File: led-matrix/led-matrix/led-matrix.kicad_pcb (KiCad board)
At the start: 4 copper layers, 300 parts, among them J1 Conn_2Rows-05Pins, Q1 2N7002, Q10 2N7002, Q11 2N7002, Q12 2N7002, Q13 2N7002, Q14 2N7002, Q15 2N7002, Q16 2N7002, Q2 2N7002, Q3 2N7002, Q4 2N7002, Q5 2N7002, Q6 2N7002, Q7 2N7002, Q8 2N7002, Q9 2N7002, U1 74LS595, U2 74LS595, U3 74LS595, U4 74LS595, U5 AMS1117-3.3

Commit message: Improved annotations and board layout
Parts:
- removed the D257 at (266.6, 236.1)
- added C5: C, Capacitor_SMD:C_0603_1608Metric, B.Cu at (26.7, 66.0)
- added C6: C, Capacitor_SMD:C_0603_1608Metric, B.Cu at (22.9, 73.7)
- added D2: LED, LED_SMD:LED_0603_1608Metric, F.Cu at (193.0, 29.2)
- added J1: Conn_2Rows-05Pins, Connector_PinHeader_1.00mm:PinHeader_1x05_P1.00mm_Horizontal, F.Cu at (7.62, 66.0)
- C1, C2, C3, C4, F1, Q11, Q6, R1, R10, R11, R12, R13, R14, R15, R16, R2, R3, R4, R5, R6, R7, R8, R9, U1, U5: moved to B.Cu
- D257: renamed from D2; moved to B.Cu
- Q1: renamed from Q16; moved to B.Cu
- Q10: renamed from Q13; moved to B.Cu
- Q12: renamed from Q9; moved to B.Cu
- Q13: renamed from Q7; moved to B.Cu
- Q14: renamed from Q5; moved to B.Cu
- Q15: renamed from Q3; moved to B.Cu
- Q16: renamed from Q1; moved to B.Cu
- Q2: renamed from Q14; moved to B.Cu
- Q3: renamed from Q12; moved to B.Cu
- Q4: renamed from Q10; moved to B.Cu
- Q5: renamed from Q8; moved to B.Cu
- Q7: renamed from Q4; moved to B.Cu
- Q8: renamed from Q2; moved to B.Cu
- Q9: renamed from Q15; moved to B.Cu
- U2: renamed from U4; moved to B.Cu
- U3: renamed from U2; moved to B.Cu
- U4: renamed from U3; moved to B.Cu
- moved D64 237.4 mm to (250.5, 44.5), turned to 90 degrees
- moved D29 236.5 mm to (232.8, 33.5), turned to 90 degrees
- moved D59 234.8 mm to (228.4, 44.5), turned to 90 degrees
- moved D47 234.6 mm to (241.3, 39.4), turned to 90 degrees
- moved D14 234.5 mm to (237.7, 29.2), turned to 90 degrees
- moved D43 234.2 mm to (226.1, 39.4), turned to 90 degrees
- moved D16 233.0 mm to (245.1, 29.2), turned to 90 degrees
- moved D24 230.0 mm to (215.2, 33.5), turned to 90 degrees
- moved D10 228.2 mm to (222.8, 29.2), turned to 90 degrees
- moved D26 228.0 mm to (222.2, 33.5), turned to 90 degrees
- moved D30 227.8 mm to (236.3, 33.5), turned to 90 degrees
- moved D36 226.7 mm to (198.1, 39.4), turned to 90 degrees
- moved D12 226.5 mm to (230.2, 29.2), turned to 90 degrees
- moved D60 226.4 mm to (232.8, 44.5), turned to 90 degrees
- moved D63 226.3 mm to (246.1, 44.5), turned to 90 degrees
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- renumbered J1 to J2
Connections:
- D105 pad 1: Net-(D10-Pad1) -> Net-(D105-Pad1)
- D106 pad 1: Net-(D106-Pad1) -> Net-(D10-Pad1)
- D11 pad 1: Net-(D104-Pad1) -> Net-(D107-Pad1)
- D113 pad 2: ROW6 -> ROW7
- D12 pad 1: Net-(D103-Pad1) -> Net-(D108-Pad1)
- D121 pad 1: Net-(D10-Pad1) -> Net-(D105-Pad1)
- D122 pad 1: Net-(D106-Pad1) -> Net-(D10-Pad1)
- D129 pad 2: ROW7 -> ROW8
- D13 pad 1: Net-(D102-Pad1) -> Net-(D109-Pad1)
- D137 pad 1: Net-(D10-Pad1) -> Net-(D105-Pad1)
- D138 pad 1: Net-(D106-Pad1) -> Net-(D10-Pad1)
- D14 pad 1: Net-(D101-Pad1) -> Net-(D110-Pad1)
- D145 pad 2: ROW8 -> ROW9
- D15 pad 1: Net-(D100-Pad1) -> Net-(D111-Pad1)
- D153 pad 1: Net-(D10-Pad1) -> Net-(D105-Pad1)
- D154 pad 1: Net-(D106-Pad1) -> Net-(D10-Pad1)
- D16 pad 1: Net-(D115-Pad1) -> Net-(D112-Pad1)
- D161 pad 2: ROW9 -> ROW10
- D169 pad 1: Net-(D10-Pad1) -> Net-(D105-Pad1)
- D17 pad 1: Net-(D114-Pad1) -> Net-(D1-Pad1)
- D17 pad 2: ROW0 -> ROW1
- D170 pad 1: Net-(D106-Pad1) -> Net-(D10-Pad1)
- D177 pad 2: ROW10 -> ROW11
- D18 pad 1: Net-(D1-Pad1) -> Net-(D114-Pad1)
- D185 pad 1: Net-(D10-Pad1) -> Net-(D105-Pad1)
- D186 pad 1: Net-(D106-Pad1) -> Net-(D10-Pad1)
- D19 pad 1: Net-(D112-Pad1) -> Net-(D115-Pad1)
- D193 pad 2: ROW11 -> ROW12
- D20 pad 1: Net-(D111-Pad1) -> Net-(D100-Pad1)
- D201 pad 1: Net-(D10-Pad1) -> Net-(D105-Pad1)
- D202 pad 1: Net-(D106-Pad1) -> Net-(D10-Pad1)
- D209 pad 2: ROW12 -> ROW13
- D21 pad 1: Net-(D110-Pad1) -> Net-(D101-Pad1)
- D217 pad 1: Net-(D10-Pad1) -> Net-(D105-Pad1)
- D218 pad 1: Net-(D106-Pad1) -> Net-(D10-Pad1)
- D22 pad 1: Net-(D109-Pad1) -> Net-(D102-Pad1)
- D225 pad 2: ROW13 -> ROW14
- D23 pad 1: Net-(D108-Pad1) -> Net-(D103-Pad1)
- D233 pad 1: Net-(D10-Pad1) -> Net-(D105-Pad1)
- D234 pad 1: Net-(D106-Pad1) -> Net-(D10-Pad1)
- D24 pad 1: Net-(D107-Pad1) -> Net-(D104-Pad1)
- D241 pad 2: ROW14 -> ROW15
- D249 pad 1: Net-(D10-Pad1) -> Net-(D105-Pad1)
- D25 pad 1: Net-(D106-Pad1) -> Net-(D105-Pad1)
- D250 pad 1: Net-(D106-Pad1) -> Net-(D10-Pad1)
- D27 pad 1: Net-(D104-Pad1) -> Net-(D107-Pad1)
- D28 pad 1: Net-(D103-Pad1) -> Net-(D108-Pad1)
- D29 pad 1: Net-(D102-Pad1) -> Net-(D109-Pad1)
- D3 pad 1: Net-(D112-Pad1) -> Net-(D115-Pad1)
- D30 pad 1: Net-(D101-Pad1) -> Net-(D110-Pad1)
- D31 pad 1: Net-(D100-Pad1) -> Net-(D111-Pad1)
- D32 pad 1: Net-(D115-Pad1) -> Net-(D112-Pad1)
- D33 pad 1: Net-(D114-Pad1) -> Net-(D1-Pad1)
- D33 pad 2: ROW1 -> ROW2
- D34 pad 1: Net-(D1-Pad1) -> Net-(D114-Pad1)
- D35 pad 1: Net-(D112-Pad1) -> Net-(D115-Pad1)
- D36 pad 1: Net-(D111-Pad1) -> Net-(D100-Pad1)
- D37 pad 1: Net-(D110-Pad1) -> Net-(D101-Pad1)
- D38 pad 1: Net-(D109-Pad1) -> Net-(D102-Pad1)
- D39 pad 1: Net-(D108-Pad1) -> Net-(D103-Pad1)
- D4 pad 1: Net-(D111-Pad1) -> Net-(D100-Pad1)
- D40 pad 1: Net-(D107-Pad1) -> Net-(D104-Pad1)
- D41 pad 1: Net-(D106-Pad1) -> Net-(D105-Pad1)
- D43 pad 1: Net-(D104-Pad1) -> Net-(D107-Pad1)
- D44 pad 1: Net-(D103-Pad1) -> Net-(D108-Pad1)
- D45 pad 1: Net-(D102-Pad1) -> Net-(D109-Pad1)
- D46 pad 1: Net-(D101-Pad1) -> Net-(D110-Pad1)
- D47 pad 1: Net-(D100-Pad1) -> Net-(D111-Pad1)
- D48 pad 1: Net-(D115-Pad1) -> Net-(D112-Pad1)
- D49 pad 1: Net-(D114-Pad1) -> Net-(D1-Pad1)
- D49 pad 2: ROW2 -> ROW3
- D5 pad 1: Net-(D110-Pad1) -> Net-(D101-Pad1)
- D50 pad 1: Net-(D1-Pad1) -> Net-(D114-Pad1)
- D51 pad 1: Net-(D112-Pad1) -> Net-(D115-Pad1)
- D52 pad 1: Net-(D111-Pad1) -> Net-(D100-Pad1)
- D53 pad 1: Net-(D110-Pad1) -> Net-(D101-Pad1)
- D54 pad 1: Net-(D109-Pad1) -> Net-(D102-Pad1)
- D55 pad 1: Net-(D108-Pad1) -> Net-(D103-Pad1)
- D56 pad 1: Net-(D107-Pad1) -> Net-(D104-Pad1)
- D57 pad 1: Net-(D106-Pad1) -> Net-(D105-Pad1)
- D59 pad 1: Net-(D104-Pad1) -> Net-(D107-Pad1)
- D6 pad 1: Net-(D109-Pad1) -> Net-(D102-Pad1)
- D60 pad 1: Net-(D103-Pad1) -> Net-(D108-Pad1)
- D61 pad 1: Net-(D102-Pad1) -> Net-(D109-Pad1)
- D62 pad 1: Net-(D101-Pad1) -> Net-(D110-Pad1)
- D63 pad 1: Net-(D100-Pad1) -> Net-(D111-Pad1)
- D64 pad 1: Net-(D115-Pad1) -> Net-(D112-Pad1)
- D65 pad 1: Net-(D114-Pad1) -> Net-(D1-Pad1)
- D65 pad 2: ROW3 -> ROW4
- D66 pad 1: Net-(D1-Pad1) -> Net-(D114-Pad1)
- D67 pad 1: Net-(D112-Pad1) -> Net-(D115-Pad1)
- D68 pad 1: Net-(D111-Pad1) -> Net-(D100-Pad1)
- D69 pad 1: Net-(D110-Pad1) -> Net-(D101-Pad1)
- D7 pad 1: Net-(D108-Pad1) -> Net-(D103-Pad1)
- D70 pad 1: Net-(D109-Pad1) -> Net-(D102-Pad1)
- D71 pad 1: Net-(D108-Pad1) -> Net-(D103-Pad1)
- D72 pad 1: Net-(D107-Pad1) -> Net-(D104-Pad1)
- D73 pad 1: Net-(D106-Pad1) -> Net-(D105-Pad1)
- D75 pad 1: Net-(D104-Pad1) -> Net-(D107-Pad1)
- D76 pad 1: Net-(D103-Pad1) -> Net-(D108-Pad1)
- D77 pad 1: Net-(D102-Pad1) -> Net-(D109-Pad1)
- D78 pad 1: Net-(D101-Pad1) -> Net-(D110-Pad1)
- D79 pad 1: Net-(D100-Pad1) -> Net-(D111-Pad1)
- D8 pad 1: Net-(D107-Pad1) -> Net-(D104-Pad1)
- D80 pad 1: Net-(D115-Pad1) -> Net-(D112-Pad1)
- D81 pad 1: Net-(D114-Pad1) -> Net-(D1-Pad1)
- D81 pad 2: ROW4 -> ROW5
- D89 pad 1: Net-(D10-Pad1) -> Net-(D105-Pad1)
- D9 pad 1: Net-(D106-Pad1) -> Net-(D105-Pad1)
- D90 pad 1: Net-(D106-Pad1) -> Net-(D10-Pad1)
- D97 pad 2: ROW5 -> ROW6
- J2 pad 1: COLNEXT -> SERCOL
- J2 pad 3: ROWSEQ -> SERROW
- R10 pad 1: Net-(D104-Pad1) -> Net-(D10-Pad1)
- R11 pad 1: Net-(D103-Pad1) -> Net-(D107-Pad1)
- R12 pad 1: Net-(D102-Pad1) -> Net-(D108-Pad1)
- R13 pad 1: Net-(D101-Pad1) -> Net-(D109-Pad1)
- R14 pad 1: Net-(D100-Pad1) -> Net-(D110-Pad1)
- R15 pad 1: Net-(D115-Pad1) -> Net-(D111-Pad1)
- R16 pad 1: Net-(D114-Pad1) -> Net-(D112-Pad1)
- R2 pad 1: Net-(D112-Pad1) -> Net-(D114-Pad1)
- R3 pad 1: Net-(D111-Pad1) -> Net-(D115-Pad1)
- R4 pad 1: Net-(D110-Pad1) -> Net-(D100-Pad1)
- R5 pad 1: Net-(D109-Pad1) -> Net-(D101-Pad1)
- R6 pad 1: Net-(D108-Pad1) -> Net-(D102-Pad1)
- R7 pad 1: Net-(D107-Pad1) -> Net-(D103-Pad1)
- R8 pad 1: Net-(D106-Pad1) -> Net-(D104-Pad1)
- R9 pad 1: Net-(D10-Pad1) -> Net-(D105-Pad1)
- U1 pad 9: Net-(U1-Pad9) -> ROWNEXT
- U3 pad 9: Net-(U2-Pad9) -> COLNEXT
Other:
- board outline added: 88.9 x 77.5 mm

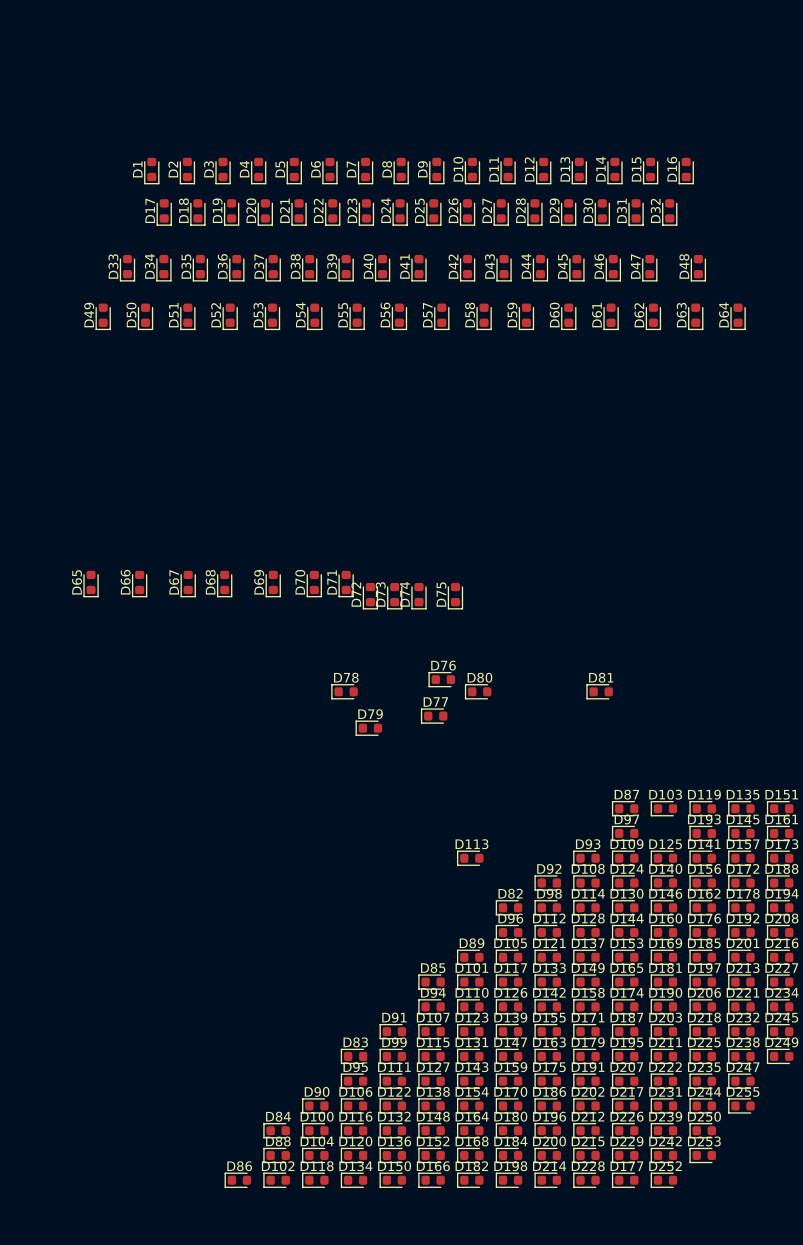
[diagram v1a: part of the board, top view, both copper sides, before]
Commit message: Updated layout
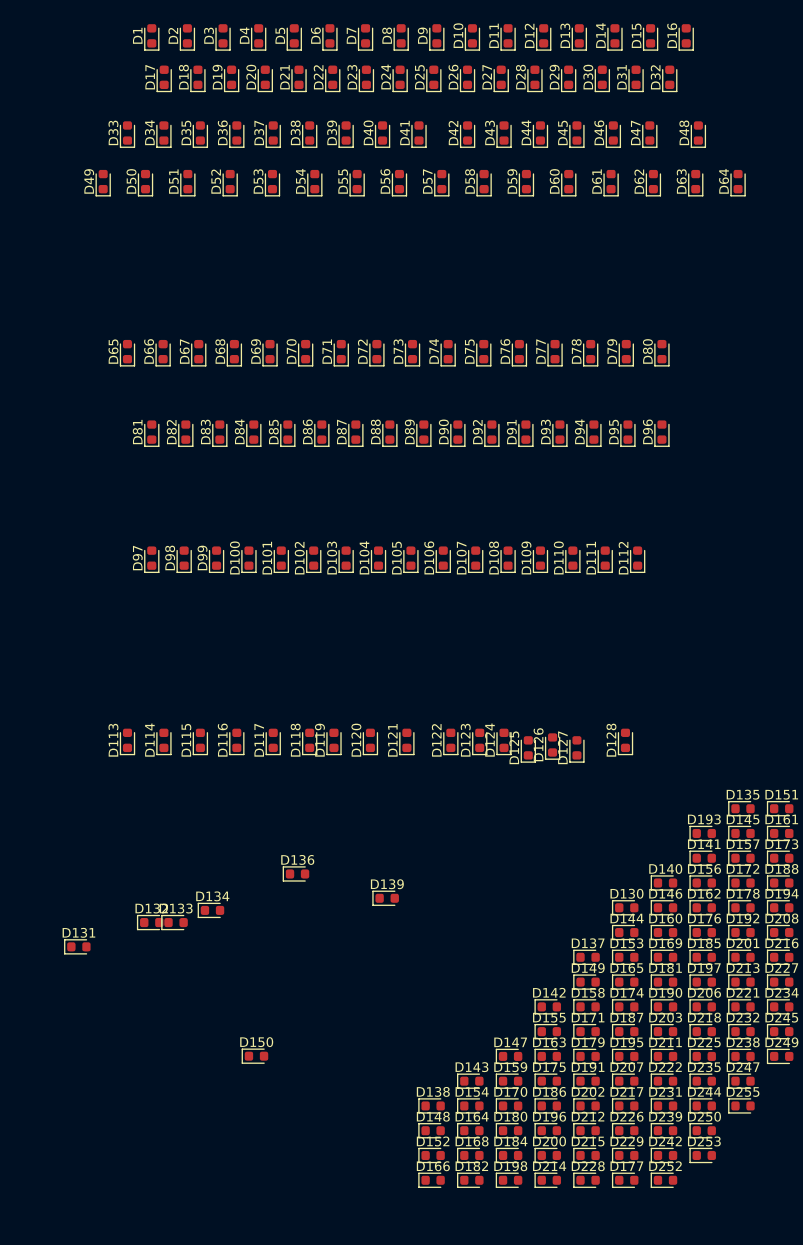
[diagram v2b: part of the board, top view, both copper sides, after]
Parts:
- moved D86 78.7 mm to (207.0, 56.7), turned to 90 degrees
- moved D88 76.5 mm to (214.1, 56.7), turned to 90 degrees
- moved D95 73.6 mm to (239.0, 56.7), turned to 90 degrees
- moved D84 73.1 mm to (199.9, 56.7), turned to 90 degrees
- moved D90 72.0 mm to (221.2, 56.7), turned to 90 degrees
- moved D83 66.8 mm to (196.3, 56.7), turned to 90 degrees
- moved D102 65.2 mm to (206.2, 69.8), turned to 90 degrees
- moved D91 64.2 mm to (228.3, 56.7), turned to 90 degrees
- moved D104 62.8 mm to (212.9, 69.8), turned to 90 degrees
- moved D94 62.4 mm to (235.5, 56.7), turned to 90 degrees
- moved D100 60.3 mm to (199.4, 69.8), turned to 90 degrees
- moved D82 60.2 mm to (192.8, 56.7), turned to 90 degrees
- moved D85 59.5 mm to (203.5, 56.7), turned to 90 degrees
- moved D111 59.0 mm to (236.6, 69.8), turned to 90 degrees
- moved D106 58.0 mm to (219.7, 69.8), turned to 90 degrees
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
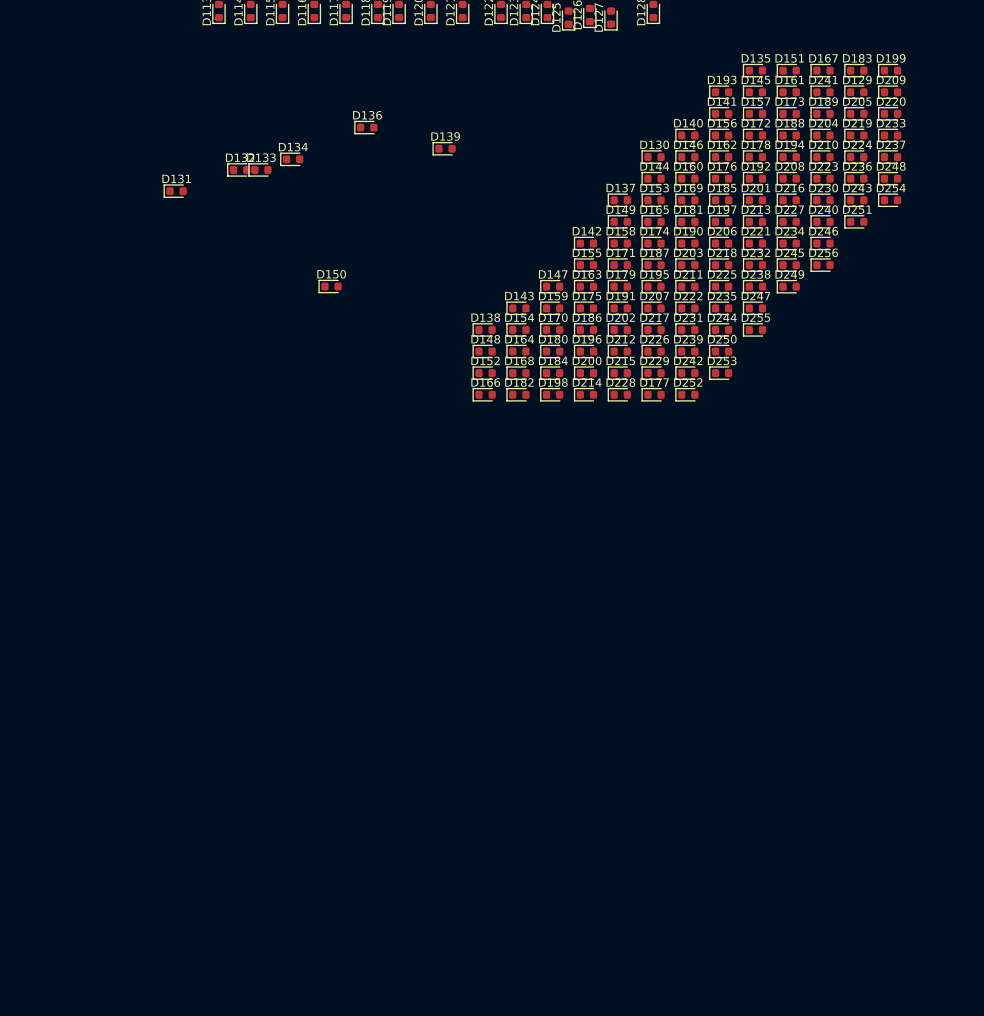
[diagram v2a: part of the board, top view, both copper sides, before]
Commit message: Updated layout grid
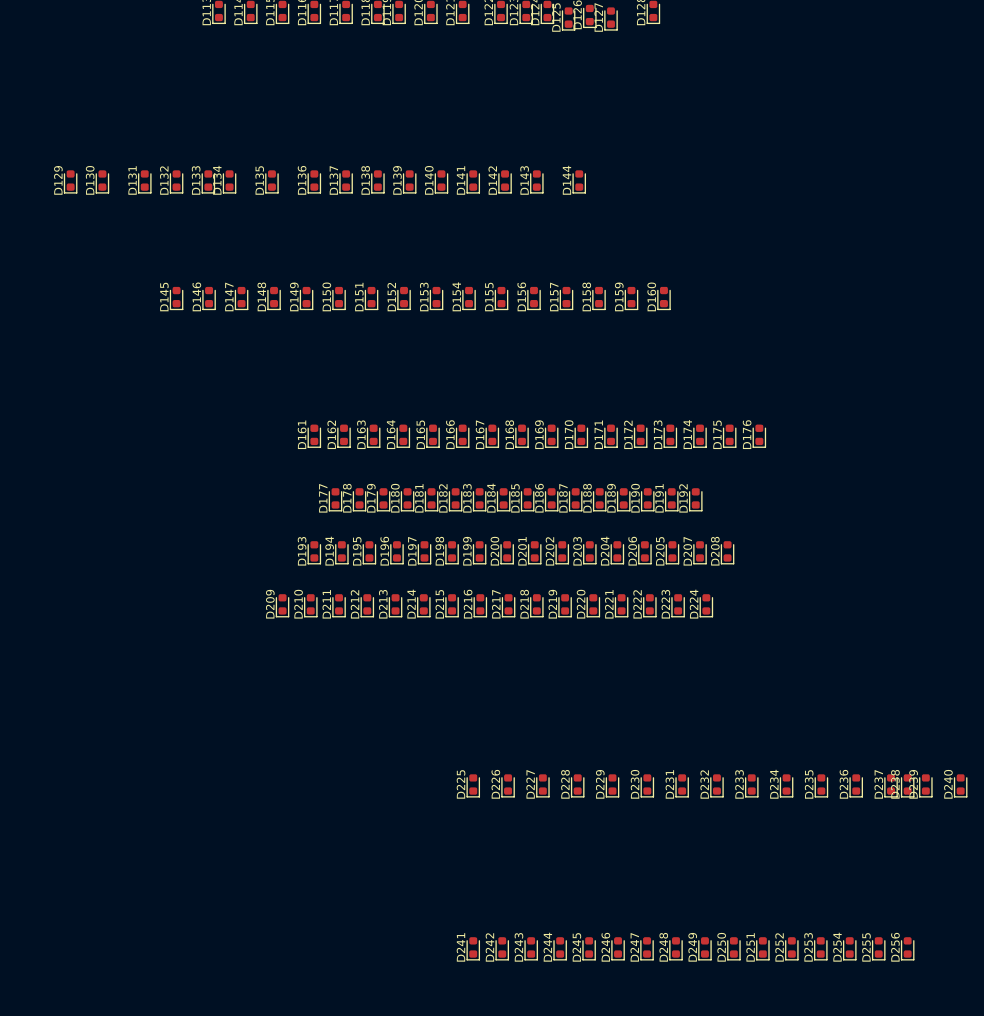
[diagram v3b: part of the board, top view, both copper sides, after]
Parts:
- moved D241 110.8 mm to (217.2, 201.1), turned to 90 degrees
- moved D243 97.7 mm to (224.1, 201.1), turned to 90 degrees
- moved D248 95.7 mm to (241.5, 201.1), turned to 90 degrees
- moved D209 95.3 mm to (194.3, 160.0), turned to 90 degrees
- moved D129 94.9 mm to (168.9, 109.2), turned to 90 degrees
- moved D254 89.7 mm to (262.3, 201.1), turned to 90 degrees
- moved D246 87.9 mm to (234.5, 201.1), turned to 90 degrees
- moved D251 87.7 mm to (251.9, 201.1), turned to 90 degrees
- moved D245 85.2 mm to (231.1, 201.1), turned to 90 degrees
- moved D256 82.4 mm to (269.2, 201.1), turned to 90 degrees
- moved D210 81.6 mm to (197.7, 160.0), turned to 90 degrees
- moved D249 79.8 mm to (244.9, 201.1), turned to 90 degrees
- moved D233 79.6 mm to (250.6, 181.6), turned to 90 degrees
- moved D247 77.7 mm to (238.0, 201.1), turned to 90 degrees
- moved D244 76.5 mm to (227.6, 201.1), turned to 90 degrees
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
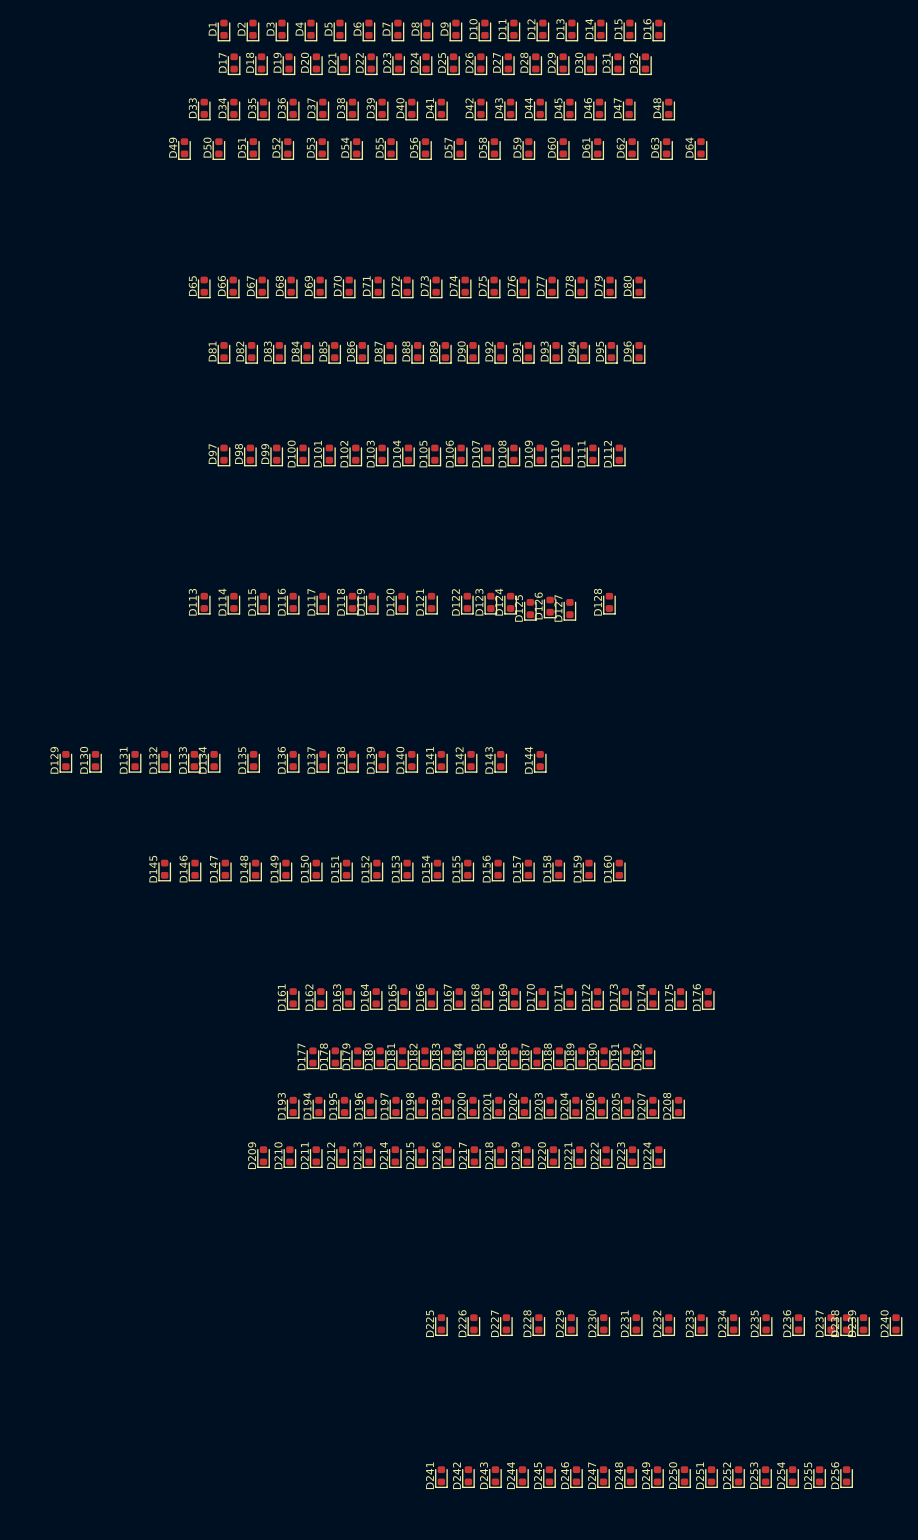
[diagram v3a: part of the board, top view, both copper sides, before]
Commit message: Setup LED matrix
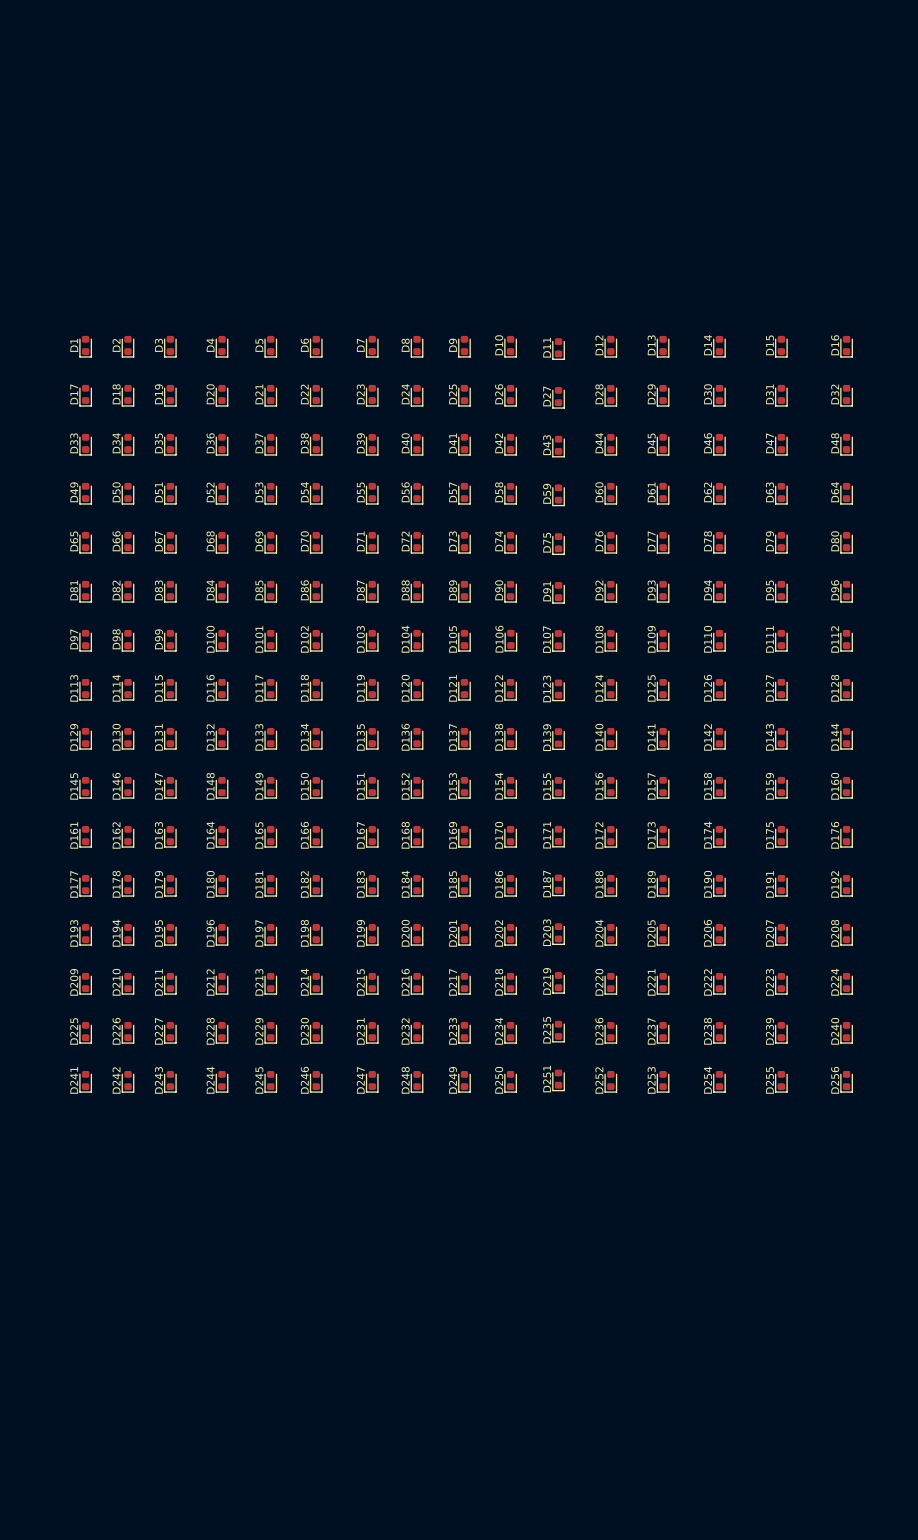
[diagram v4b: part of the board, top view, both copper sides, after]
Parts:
- moved D241 68.3 mm to (171.4, 150.3)
- moved D242 67.0 mm to (176.9, 150.3)
- moved D243 65.8 mm to (182.3, 150.3)
- moved D244 63.8 mm to (189.0, 150.3)
- moved D245 62.2 mm to (195.2, 150.3)
- moved D246 60.8 mm to (201.1, 150.3)
- moved D225 59.2 mm to (171.4, 144.0)
- moved D247 58.9 mm to (208.3, 150.3)
- moved D226 58.2 mm to (176.9, 144.0)
- moved D248 57.7 mm to (214.0, 150.3)
- moved D227 57.2 mm to (182.3, 144.0)
- moved D249 56.5 mm to (220.1, 150.3)
- moved D250 55.5 mm to (226.1, 150.3)
- moved D228 55.4 mm to (189.0, 144.0)
- moved D251 54.6 mm to (232.2, 150.2)
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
